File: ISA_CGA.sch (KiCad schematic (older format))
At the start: 32 parts, among them U1 74S112, U11 74LS74, U12 74LS393, U13 74LS08, U14 74S32, U15 74LS00, U16 74LS04, U2 74LS74, U20 74LS04, U22 74LS51, U23 74LS32, U24 74LS244, U25 74LS00, U26 74S04, U27 74LS51, U28 74LS10, U29 74S04, U3 74S86, U30 74LS32, U31 74S08, U41 74LS08, U42 74LS86, U43 74S74, U44 74S74, U46 74LS00, U47 74LS51, U48 74LS51, U49 74LS02, U6 74LS04, U62 74LS125, U65 74LS02, U68 74LS86

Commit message: Changed footprints, moving components
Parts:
- U1: footprint Package_DIP:DIP-16_W7.62mm_LongPads -> Package_DIP:DIP-16_W7.62mm
- U11, U12, U13, U14, U15, U16, U2, U20, U22, U23, U25, U26, U27, U28, U29, U3, U30, U31, U41, U42, U43, U44, U46, U47, U48, U6, U62, U65, U68: footprint Package_DIP:DIP-14_W7.62mm_LongPads -> Package_DIP:DIP-14_W7.62mm
- U24: footprint Package_DIP:DIP-20_W7.62mm_LongPads -> Package_DIP:DIP-20_W7.62mm
- U49: footprint (none) -> Package_DIP:DIP-14_W7.62mm
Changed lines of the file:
@@
 F 0 "U48" H 6850 5550 50  0000 C CNN
 F 1 "74LS51" H 7150 5550 50  0000 C CNN
-F 2 "Package_DIP:DIP-14_W7.62mm_LongPads" H 7000 5200 50  0001 C CNN
+F 2 "Package_DIP:DIP-14_W7.62mm" H 7000 5200 50  0001 C CNN
 F 3 "http://www.ti.com/lit/ds/symlink/sn74ls51.pdf" H 7000 5200 50  0001 C CNN
 	3    7000 5200
@@
 F 0 "U49" H 7500 5550 50  0000 C CNN
 F 1 "74LS02" H 7750 5550 50  0000 C CNN
-F 2 "" H 7600 5200 50  0001 C CNN
+F 2 "Package_DIP:DIP-14_W7.62mm" H 7600 5200 50  0001 C CNN
 F 3 "http://www.ti.com/lit/gpn/sn74ls02" H 7600 5200 50  0001 C CNN
 	5    7600 5200
@@
 F 0 "U62" H 8050 5550 50  0000 C CNN
 F 1 "74LS125" H 8400 5550 50  0000 C CNN
-F 2 "Package_DIP:DIP-14_W7.62mm_LongPads" H 8200 5200 50  0001 C CNN
+F 2 "Package_DIP:DIP-14_W7.62mm" H 8200 5200 50  0001 C CNN
 F 3 "http://www.ti.com/lit/gpn/sn74LS125" H 8200 5200 50  0001 C CNN
 	5    8200 5200
@@
 F 0 "U13" H 4400 3700 50  0000 R CNN
 F 1 "74LS08" H 4800 3700 50  0000 R CNN
-F 2 "Package_DIP:DIP-14_W7.62mm_LongPads" H 4500 3350 50  0001 C CNN
+F 2 "Package_DIP:DIP-14_W7.62mm" H 4500 3350 50  0001 C CNN
 F 3 "http://www.ti.com/lit/gpn/sn74LS08" H 4500 3350 50  0001 C CNN
 	5    4500 3350
@@
 F 0 "U28" H 650 5550 50  0000 L CNN
 F 1 "74LS10" H 900 5550 50  0000 L CNN
-F 2 "Package_DIP:DIP-14_W7.62mm_LongPads" H 900 5200 50  0001 C CNN
+F 2 "Package_DIP:DIP-14_W7.62mm" H 900 5200 50  0001 C CNN
 F 3 "http://www.ti.com/lit/gpn/sn74LS10" H 900 5200 50  0001 C CNN
 	4    900  5200
@@
 F 0 "U14" H 5050 3700 50  0000 R CNN
 F 1 "74S32" H 5400 3700 50  0000 R CNN
-F 2 "Package_DIP:DIP-14_W7.62mm_LongPads" H 5100 3350 50  0001 C CNN
+F 2 "Package_DIP:DIP-14_W7.62mm" H 5100 3350 50  0001 C CNN
 F 3 "http://www.ti.com/lit/gpn/sn74LS32" H 5100 3350 50  0001 C CNN
 	5    5100 3350
@@
 F 0 "U68" H 9300 5550 50  0000 C CNN
 F 1 "74LS86" H 9550 5550 50  0000 C CNN
-F 2 "Package_DIP:DIP-14_W7.62mm_LongPads" H 9400 5200 50  0001 C CNN
+F 2 "Package_DIP:DIP-14_W7.62mm" H 9400 5200 50  0001 C CNN
 F 3 "74xx/74ls86.pdf" H 9400 5200 50  0001 C CNN
 	5    9400 5200
@@
 F 0 "U31" H 2550 5550 50  0000 C CNN
 F 1 "74S08" H 2850 5550 50  0000 C CNN
-F 2 "Package_DIP:DIP-14_W7.62mm_LongPads" H 2700 5200 50  0001 C CNN
+F 2 "Package_DIP:DIP-14_W7.62mm" H 2700 5200 50  0001 C CNN
 F 3 "http://www.ti.com/lit/gpn/sn74LS08" H 2700 5200 50  0001 C CNN
 	5    2700 5200
@@
 F 0 "U6" H 2550 3700 50  0000 C CNN
 F 1 "74LS04" H 2850 3700 50  0000 C CNN
-F 2 "Package_DIP:DIP-14_W7.62mm_LongPads" H 2700 3350 50  0001 C CNN
+F 2 "Package_DIP:DIP-14_W7.62mm" H 2700 3350 50  0001 C CNN
 F 3 "http://www.ti.com/lit/gpn/sn74LS04" H 2700 3350 50  0001 C CNN
 	7    2700 3350
@@
 F 0 "U42" H 4050 5550 50  0000 C CNN
 F 1 "74LS86" H 3750 5550 50  0000 C CNN
-F 2 "Package_DIP:DIP-14_W7.62mm_LongPads" H 3900 5200 50  0001 C CNN
+F 2 "Package_DIP:DIP-14_W7.62mm" H 3900 5200 50  0001 C CNN
 F 3 "74xx/74ls86.pdf" H 3900 5200 50  0001 C CNN
 	5    3900 5200
@@
 F 0 "U3" H 1950 3700 50  0000 C CNN
 F 1 "74S86" H 2250 3700 50  0000 C CNN
-F 2 "Package_DIP:DIP-14_W7.62mm_LongPads" H 2100 3350 50  0001 C CNN
+F 2 "Package_DIP:DIP-14_W7.62mm" H 2100 3350 50  0001 C CNN
 F 3 "74xx/74ls86.pdf" H 2100 3350 50  0001 C CNN
 	5    2100 3350
@@
 F 0 "U30" H 1950 5550 50  0000 C CNN
 F 1 "74LS32" H 2250 5550 50  0000 C CNN
-F 2 "Package_DIP:DIP-14_W7.62mm_LongPads" H 2100 5200 50  0001 C CNN
+F 2 "Package_DIP:DIP-14_W7.62mm" H 2100 5200 50  0001 C CNN
 F 3 "http://www.ti.com/lit/gpn/sn74LS32" H 2100 5200 50  0001 C CNN
 	5    2100 5200
@@
 F 0 "U1" H 750 3700 50  0000 C CNN
 F 1 "74S112" H 1100 3700 50  0000 C CNN
-F 2 "Package_DIP:DIP-16_W7.62mm_LongPads" H 900 3350 50  0001 C CNN
+F 2 "Package_DIP:DIP-16_W7.62mm" H 900 3350 50  0001 C CNN
 F 3 "http://www.ti.com/lit/gpn/sn74LS112" H 900 3350 50  0001 C CNN
 	3    900  3350
@@
 F 0 "U12" H 3650 3700 50  0000 L CNN
 F 1 "74LS393" H 3900 3700 50  0000 L CNN
-F 2 "Package_DIP:DIP-14_W7.62mm_LongPads" H 3900 3350 50  0001 C CNN
+F 2 "Package_DIP:DIP-14_W7.62mm" H 3900 3350 50  0001 C CNN
 F 3 "74xx\\74LS393.pdf" H 3900 3350 50  0001 C CNN
 	3    3900 3350
@@
 F 0 "U11" H 3150 3700 50  0000 C CNN
 F 1 "74LS74" H 3500 3700 50  0000 C CNN
-F 2 "Package_DIP:DIP-14_W7.62mm_LongPads" H 3300 3350 50  0001 C CNN
+F 2 "Package_DIP:DIP-14_W7.62mm" H 3300 3350 50  0001 C CNN
 F 3 "74xx/74hc_hct74.pdf" H 3300 3350 50  0001 C CNN
 	3    3300 3350
@@
 F 0 "U15" H 5500 3700 50  0000 L CNN
 F 1 "74LS00" H 5700 3700 50  0000 L CNN
-F 2 "Package_DIP:DIP-14_W7.62mm_LongPads" H 5700 3350 50  0001 C CNN
+F 2 "Package_DIP:DIP-14_W7.62mm" H 5700 3350 50  0001 C CNN
 F 3 "http://www.ti.com/lit/gpn/sn74ls00" H 5700 3350 50  0001 C CNN
 	5    5700 3350
@@
 F 0 "U16" H 6150 3700 50  0000 C CNN
 F 1 "74LS04" H 6450 3700 50  0000 C CNN
-F 2 "Package_DIP:DIP-14_W7.62mm_LongPads" H 6300 3350 50  0001 C CNN
+F 2 "Package_DIP:DIP-14_W7.62mm" H 6300 3350 50  0001 C CNN
 F 3 "http://www.ti.com/lit/gpn/sn74LS04" H 6300 3350 50  0001 C CNN
 	7    6300 3350
@@
 F 0 "U65" H 8600 5550 50  0000 L CNN
 F 1 "74LS02" H 8800 5550 50  0000 L CNN
-F 2 "Package_DIP:DIP-14_W7.62mm_LongPads" H 8800 5200 50  0001 C CNN
+F 2 "Package_DIP:DIP-14_W7.62mm" H 8800 5200 50  0001 C CNN
 F 3 "http://www.ti.com/lit/gpn/sn74ls02" H 8800 5200 50  0001 C CNN
 	5    8800 5200
@@
 F 0 "U41" H 3150 5550 50  0000 C CNN
 F 1 "74LS08" H 3450 5550 50  0000 C CNN
-F 2 "Package_DIP:DIP-14_W7.62mm_LongPads" H 3300 5200 50  0001 C CNN
+F 2 "Package_DIP:DIP-14_W7.62mm" H 3300 5200 50  0001 C CNN
 F 3 "http://www.ti.com/lit/gpn/sn74LS08" H 3300 5200 50  0001 C CNN
 	5    3300 5200
@@
 F 0 "U26" H 9850 3700 50  0000 C CNN
 F 1 "74S04" H 10150 3700 50  0000 C CNN
-F 2 "Package_DIP:DIP-14_W7.62mm_LongPads" H 10000 3350 50  0001 C CNN
+F 2 "Package_DIP:DIP-14_W7.62mm" H 10000 3350 50  0001 C CNN
 F 3 "http://www.ti.com/lit/gpn/sn74LS04" H 10000 3350 50  0001 C CNN
 	7    10000 3350
@@
 F 0 "U22" H 7450 3700 50  0000 R CNN
 F 1 "74LS51" H 7800 3700 50  0000 R CNN
-F 2 "Package_DIP:DIP-14_W7.62mm_LongPads" H 7500 3350 50  0001 C CNN
+F 2 "Package_DIP:DIP-14_W7.62mm" H 7500 3350 50  0001 C CNN
 F 3 "http://www.ti.com/lit/ds/symlink/sn74ls51.pdf" H 7500 3350 50  0001 C CNN
 	3    7500 3350
@@
 F 0 "U29" H 1350 5550 50  0000 C CNN
 F 1 "74S04" H 1650 5550 50  0000 C CNN
-F 2 "Package_DIP:DIP-14_W7.62mm_LongPads" H 1500 5200 50  0001 C CNN
+F 2 "Package_DIP:DIP-14_W7.62mm" H 1500 5200 50  0001 C CNN
 F 3 "http://www.ti.com/lit/gpn/sn74LS04" H 1500 5200 50  0001 C CNN
 	7    1500 5200
@@
 F 0 "U25" H 9250 3700 50  0000 C CNN
 F 1 "74LS00" H 9550 3700 50  0000 C CNN
-F 2 "Package_DIP:DIP-14_W7.62mm_LongPads" H 9400 3350 50  0001 C CNN
+F 2 "Package_DIP:DIP-14_W7.62mm" H 9400 3350 50  0001 C CNN
 F 3 "http://www.ti.com/lit/gpn/sn74ls00" H 9400 3350 50  0001 C CNN
 	5    9400 3350
@@
 F 0 "U27" H 10350 3700 50  0000 L CNN
 F 1 "74LS51" H 10600 3700 50  0000 L CNN
-F 2 "Package_DIP:DIP-14_W7.62mm_LongPads" H 10600 3350 50  0001 C CNN
+F 2 "Package_DIP:DIP-14_W7.62mm" H 10600 3350 50  0001 C CNN
 F 3 "http://www.ti.com/lit/ds/symlink/sn74ls51.pdf" H 10600 3350 50  0001 C CNN
 	3    10600 3350
@@
 F 0 "U2" H 1350 3700 50  0000 C CNN
 F 1 "74LS74" H 1650 3700 50  0000 C CNN
-F 2 "Package_DIP:DIP-14_W7.62mm_LongPads" H 1500 3350 50  0001 C CNN
+F 2 "Package_DIP:DIP-14_W7.62mm" H 1500 3350 50  0001 C CNN
 F 3 "74xx/74hc_hct74.pdf" H 1500 3350 50  0001 C CNN
 	3    1500 3350
@@
 F 0 "U20" H 6750 3700 50  0000 C CNN
 F 1 "74LS04" H 7050 3700 50  0000 C CNN
-F 2 "Package_DIP:DIP-14_W7.62mm_LongPads" H 6900 3350 50  0001 C CNN
+F 2 "Package_DIP:DIP-14_W7.62mm" H 6900 3350 50  0001 C CNN
 F 3 "http://www.ti.com/lit/gpn/sn74LS04" H 6900 3350 50  0001 C CNN
 	7    6900 3350
@@
 F 0 "U23" H 7850 3700 50  0000 L CNN
 F 1 "74LS32" H 8150 3700 50  0000 L CNN
-F 2 "Package_DIP:DIP-14_W7.62mm_LongPads" H 8100 3350 50  0001 C CNN
+F 2 "Package_DIP:DIP-14_W7.62mm" H 8100 3350 50  0001 C CNN
 F 3 "http://www.ti.com/lit/gpn/sn74LS32" H 8100 3350 50  0001 C CNN
 	5    8100 3350
@@
 F 0 "U47" H 6150 5550 50  0000 L CNN
 F 1 "74LS51" H 6450 5550 50  0000 L CNN
-F 2 "Package_DIP:DIP-14_W7.62mm_LongPads" H 6400 5200 50  0001 C CNN
+F 2 "Package_DIP:DIP-14_W7.62mm" H 6400 5200 50  0001 C CNN
 F 3 "http://www.ti.com/lit/ds/symlink/sn74ls51.pdf" H 6400 5200 50  0001 C CNN
 	3    6400 5200
@@
 F 0 "U43" H 4400 5550 50  0000 C CNN
 F 1 "74S74" H 4700 5550 50  0000 C CNN
-F 2 "Package_DIP:DIP-14_W7.62mm_LongPads" H 4550 5200 50  0001 C CNN
+F 2 "Package_DIP:DIP-14_W7.62mm" H 4550 5200 50  0001 C CNN
 F 3 "74xx/74hc_hct74.pdf" H 4550 5200 50  0001 C CNN
 	3    4550 5200
@@
 F 0 "U24" H 8550 3700 50  0000 L CNN
 F 1 "74LS244" H 8750 3700 50  0000 L CNN
-F 2 "Package_DIP:DIP-20_W7.62mm_LongPads" H 8750 3350 50  0001 C CNN
+F 2 "Package_DIP:DIP-20_W7.62mm" H 8750 3350 50  0001 C CNN
 F 3 "http://www.ti.com/lit/ds/symlink/sn74ls241.pdf" H 8750 3350 50  0001 C CNN
 	9    8750 3350
@@
 F 0 "U46" H 5650 5550 50  0000 C CNN
 F 1 "74LS00" H 5950 5550 50  0000 C CNN
-F 2 "Package_DIP:DIP-14_W7.62mm_LongPads" H 5800 5200 50  0001 C CNN
+F 2 "Package_DIP:DIP-14_W7.62mm" H 5800 5200 50  0001 C CNN
 F 3 "http://www.ti.com/lit/gpn/sn74ls00" H 5800 5200 50  0001 C CNN
 	5    5800 5200
@@
 F 0 "U44" H 5050 5550 50  0000 C CNN
 F 1 "74S74" H 5350 5550 50  0000 C CNN
-F 2 "Package_DIP:DIP-14_W7.62mm_LongPads" H 5200 5200 50  0001 C CNN
+F 2 "Package_DIP:DIP-14_W7.62mm" H 5200 5200 50  0001 C CNN
 F 3 "74xx/74hc_hct74.pdf" H 5200 5200 50  0001 C CNN
 	3    5200 5200

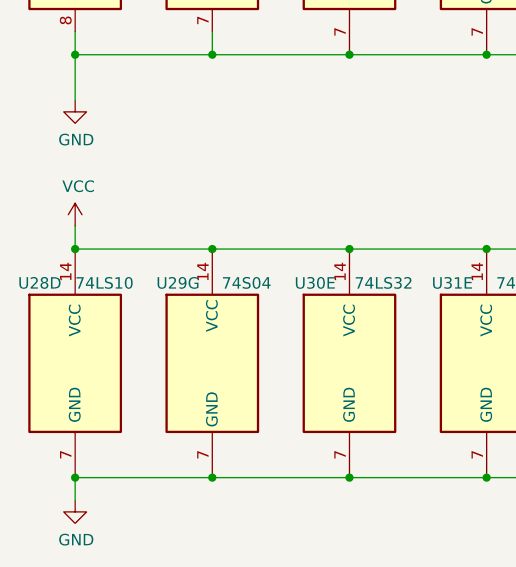
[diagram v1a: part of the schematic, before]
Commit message: Replaced 74LS10 for U28 with 74S10
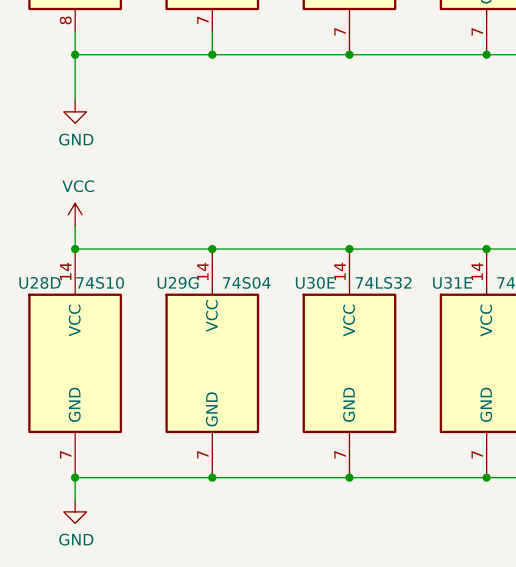
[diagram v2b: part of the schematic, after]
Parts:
- U28: value 74LS10 -> 74S10
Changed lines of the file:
@@
 AR Path="/6073B547" Ref="U28"  Part="4"
 F 0 "U28" H 650 5550 50  0000 L CNN
-F 1 "74LS10" H 900 5550 50  0000 L CNN
+F 1 "74S10" H 900 5550 50  0000 L CNN
 F 2 "Package_DIP:DIP-14_W7.62mm" H 900 5200 50  0001 C CNN
 F 3 "http://www.ti.com/lit/gpn/sn74LS10" H 900 5200 50  0001 C CNN
